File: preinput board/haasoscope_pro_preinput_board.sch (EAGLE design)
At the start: 44 parts, among them J1 test1, J2 8pin, J4 8pin, K1 AQY21SOP, K2 G6K-2F-RF-DC3, K3 G6K-2F-RF-DC3, K4 G6K-2F-RF-DC3, Q1 S8050, Q2 S8050, Q3 S8050

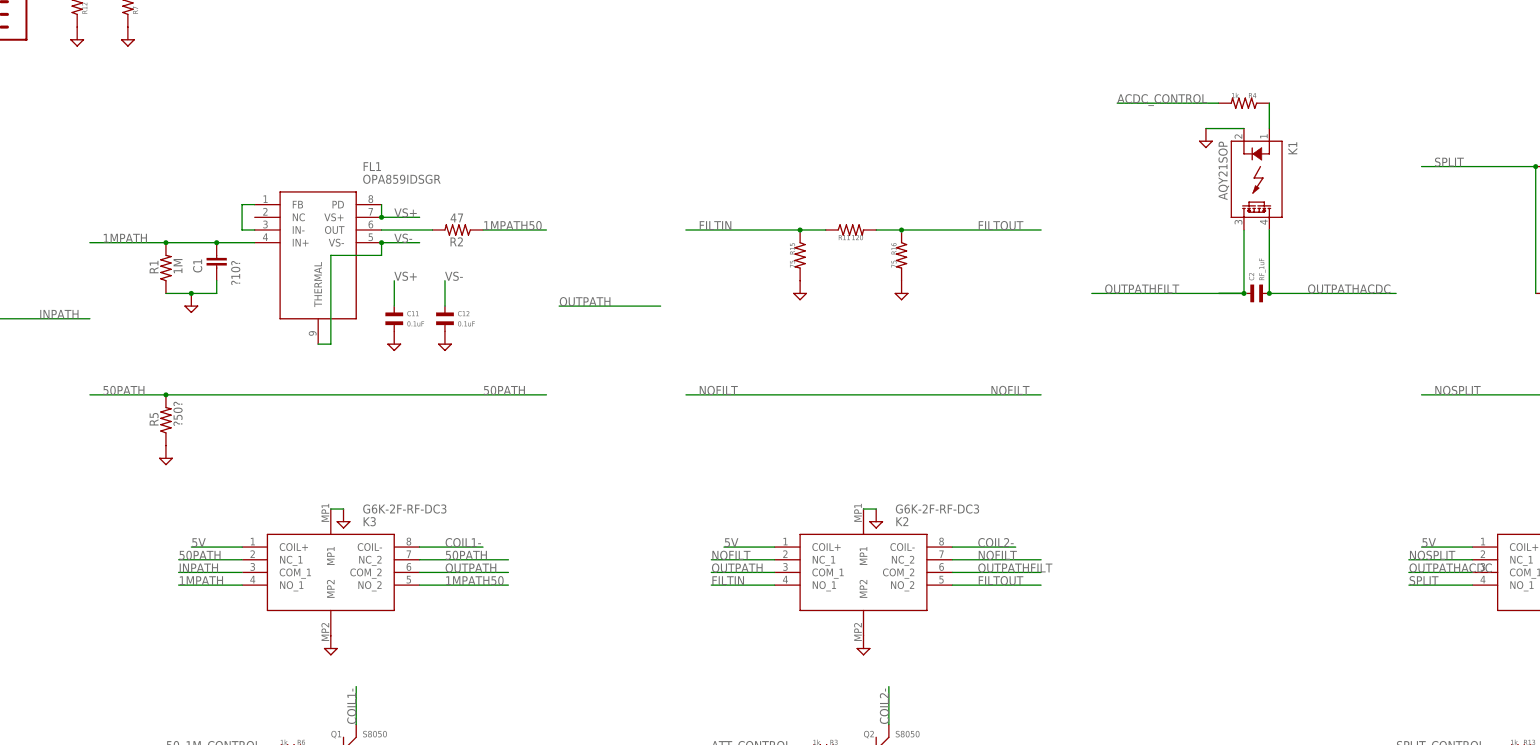
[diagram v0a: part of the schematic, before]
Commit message: add -T relay, and new ACDC SSR
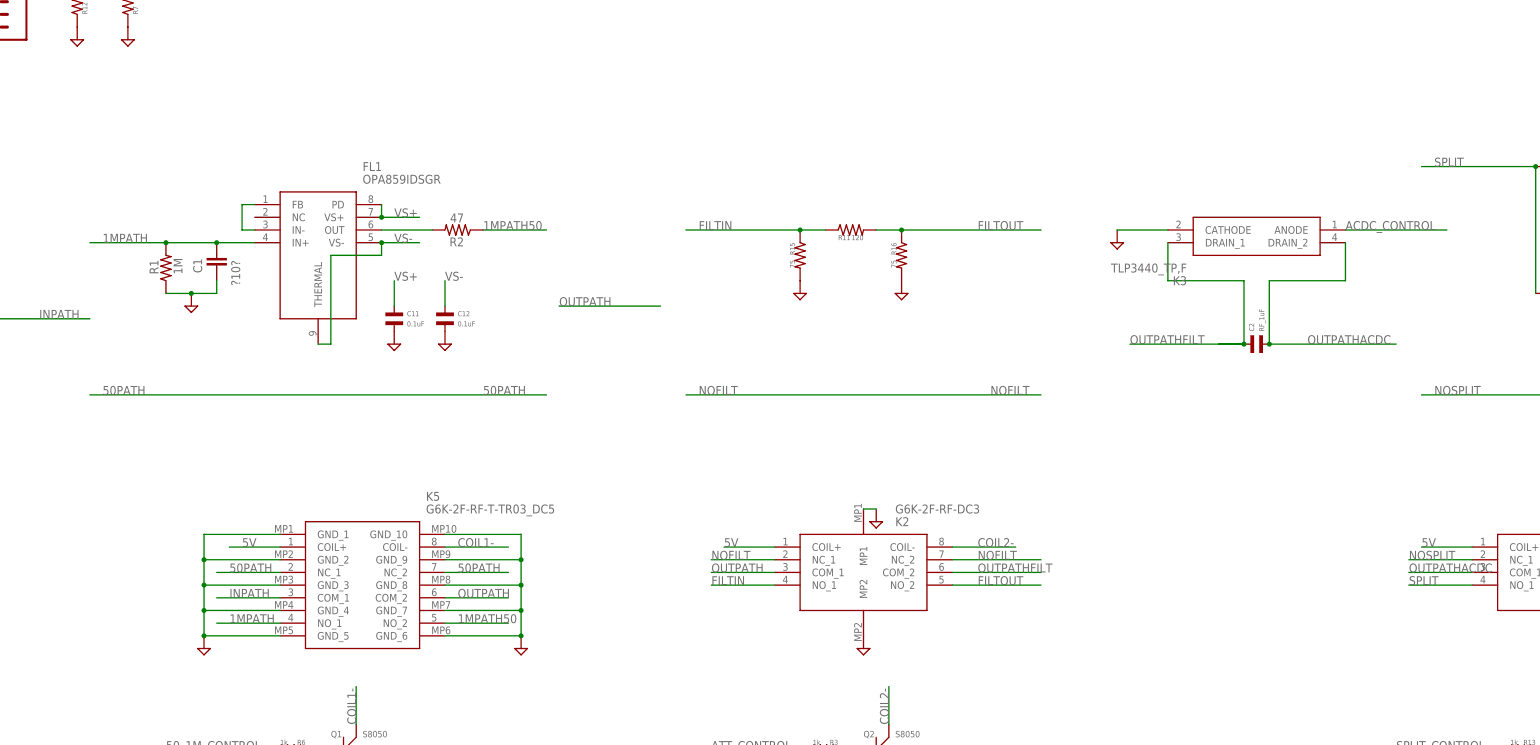
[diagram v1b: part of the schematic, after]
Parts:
- removed K1: AQY21SOP, relay:AQY21SOP
- removed R4: 1k, MF_Passives:RESISTOR_0402
- removed R5: ?50?, resistor:R-US_R0805
- added K5: G6K-2F-RF-T-TR03_DC5, G6K-2F-RF-T-TR03_DC5:G6K-2F-RF-T-TR03_DC5
- K3: value G6K-2F-RF-DC3 -> TLP3440_TP,F; device G6K-2F-RF-DC3:G6K-2F-RF-DC3 -> TLP3440_TP_F:TLP3440_TP,F; LCSC C397195 -> (none); MANUFACTURER_PART_NUMBER (none) -> TLP3475R(TP,F
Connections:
- removed net N$11: K1.A, R4.P$1
- net 1MPATH: now also K5.NO_1; no longer K3.NO_1
- net 1MPATH50: now also K5.NO_2; no longer K3.NO_2
- net 50PATH: now also K5.NC_1, K5.NC_2; no longer K3.NC_1, K3.NC_2, R5.2
- net 5V: now also K5.COIL+; no longer K3.COIL+
- net ACDC_CONTROL: now also K3.ANODE; no longer R4.P$2
- net COIL1-: now also K5.COIL-; no longer K3.COIL-
- net GND: now also K3.CATHODE, K5.GND_1, K5.GND_10, K5.GND_2, K5.GND_3, K5.GND_4, K5.GND_5, K5.GND_6, K5.GND_7, K5.GND_8, K5.GND_9; no longer K1.K, K3.MP1, K3.MP2, R5.1
- net INPATH: now also K5.COM_1; no longer K3.COM_1
- net OUTPATH: now also K5.COM_2; no longer K3.COM_2
- net OUTPATHACDC: now also K3.DRAIN_2; no longer K1.DS1
- net OUTPATHFILT: now also K3.DRAIN_1; no longer K1.DS2
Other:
- moved on the sheet: C2

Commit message: use new T relays, re-layout
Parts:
- removed C3: 1uF, MF_Passives:CAPACITOR_NP_0402
- removed J1: test1, FlashPCB_Connectors:USB-TYPE-ATHT-RA
- removed J2: 8pin, SparkFun-Connectors:CONN_08"
- removed K4: G6K-2F-RF-DC3, G6K-2F-RF-DC3:G6K-2F-RF-DC3
- removed R14: 0, MF_Passives:RESISTOR_0402
- removed TESTBNC1, TESTBNC2: MOLEX_BNC_73100-0105, connector:MOLEX_BNC_73100-0105
- removed TESTSMA1, TESTSMA2, TESTSMA3, TESTSMA4: out50, adafruit:SMACONNECTOR_EDGE
- removed U$1: RJ45-CONNECTOR-SHIELDED, FlashPCB_Connectors:RJ45-CONNECTOR-SHIELDED
- added K1: G6K-2F-RF-T-TR03_DC5, G6K-2F-RF-T-TR03_DC5:G6K-2F-RF-T-TR03_DC5
- K2: value G6K-2F-RF-DC3 -> G6K-2F-RF-T-TR03_DC5; device G6K-2F-RF-DC3:G6K-2F-RF-DC3 -> G6K-2F-RF-T-TR03_DC5:G6K-2F-RF-T-TR03_DC5; LCSC C397195 -> (none)
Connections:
- removed net DA_N: J2.2, U$1.2
- removed net DA_P: J2.1, U$1.1
- removed net DB_N: J2.4, U$1.6
- removed net DB_P: J2.3, U$1.3
- removed net DC_N: J2.6, U$1.5
- removed net DC_P: J2.5, U$1.4
- removed net DD_N: J2.8, U$1.8
- removed net DD_P: J2.7, U$1.7
- removed net N$10: R14.P$2, TESTSMA3.ANT
- removed net N$12: C3.P$1, R14.P$1
- removed net N$13: C3.P$2, TESTSMA4.ANT
- removed net N$8: TESTBNC1.SIGNAL, TESTBNC2.SIGNAL
- removed net N$9: TESTSMA1.ANT, TESTSMA2.ANT
- removed net OUTPATHACDC: C2.P$2, K3.DRAIN_2, K4.COM_1
- new net OUTSPLITTER: K1.COM_2, K5.COM_1
- net 5V: now also K1.COIL+; no longer J1.VCC, K4.COIL+
- net COIL3-: now also K1.COIL-; no longer K4.COIL-
- net GND: now also K1.GND_1, K1.GND_10, K1.GND_2, K1.GND_3, K1.GND_4, K1.GND_5, K1.GND_6, K1.GND_7, K1.GND_8, K1.GND_9, K2.GND_1, K2.GND_10, K2.GND_2, K2.GND_3, K2.GND_4, K2.GND_5, K2.GND_6, K2.GND_7, K2.GND_8, K2.GND_9; no longer J1.GND, K2.MP1, K2.MP2, K4.MP1, K4.MP2, TESTBNC1.GND, TESTBNC2.GND, TESTSMA1.GND1, TESTSMA1.GND2, TESTSMA1.GND3, TESTSMA1.GND4, TESTSMA2.GND1, TESTSMA2.GND2, TESTSMA2.GND3, TESTSMA2.GND4, TESTSMA3.GND1, TESTSMA3.GND2, TESTSMA3.GND3, TESTSMA3.GND4, TESTSMA4.GND1, TESTSMA4.GND2, TESTSMA4.GND3, TESTSMA4.GND4, U$1.SHIELD
- net INPATH: now also K1.COM_1; no longer K5.COM_1
- net NOSPLIT: now also K1.NC_1, K1.NC_2; no longer K4.NC_1, K4.NC_2
- net OUTMAIN: now also C2.P$2, K3.DRAIN_2; no longer K4.COM_2
- net SPLIT: now also K1.NO_1; no longer K4.NO_1
- net SPLITOUT: now also K1.NO_2; no longer K4.NO_2
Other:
- note added: "Inputs and controls"
- moved on the sheet: BNCIN, D1, D2, OUTMAIN, OUTSPLIT, Q3, R10, R12, R13, R7, R8, R9

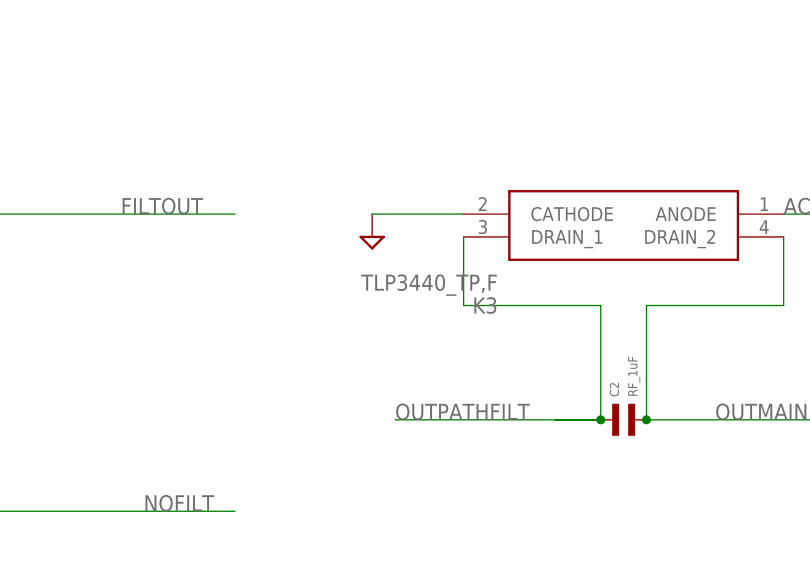
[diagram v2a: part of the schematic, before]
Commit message: rename photoMOS to 3475R
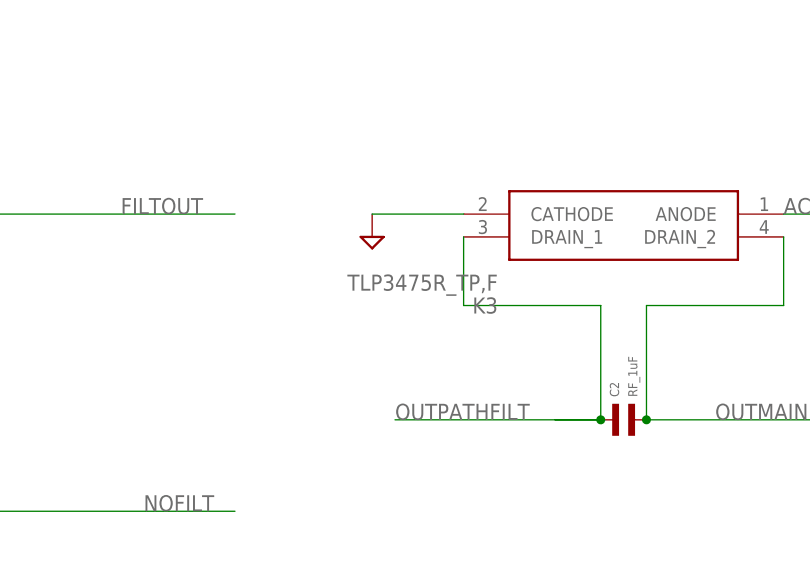
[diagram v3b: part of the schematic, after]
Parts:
- K3: value TLP3440_TP,F -> TLP3475R_TP,F; device TLP3440_TP_F:TLP3440_TP,F -> TLP3475R_TP_F:TLP3475R_TP,F
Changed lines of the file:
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@@
 <part name="K5" library="G6K-2F-RF-T-TR03_DC5" deviceset="G6K-2F-RF-T-TR03_DC5" device=""/>
 <part name="SUPPLY9" library="supply2" library_urn="urn:adsk.eagle:library:372" deviceset="GND" device=""/>
-<part name="K3" library="TLP3440_TP_F" deviceset="TLP3440_TP,F" device="">
+<part name="K3" library="TLP3475R_TP_F" deviceset="TLP3475R_TP,F" device="">
 <attribute name="MANUFACTURER_PART_NUMBER" value="TLP3475R(TP,F"/>
 </part>
